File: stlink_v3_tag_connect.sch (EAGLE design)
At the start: 10 parts, among them CON1 STLINK_V3_HAT_SWD/JTAG_MINIMAL, J1 RJ12, U1 SN74LVC2T45DCU

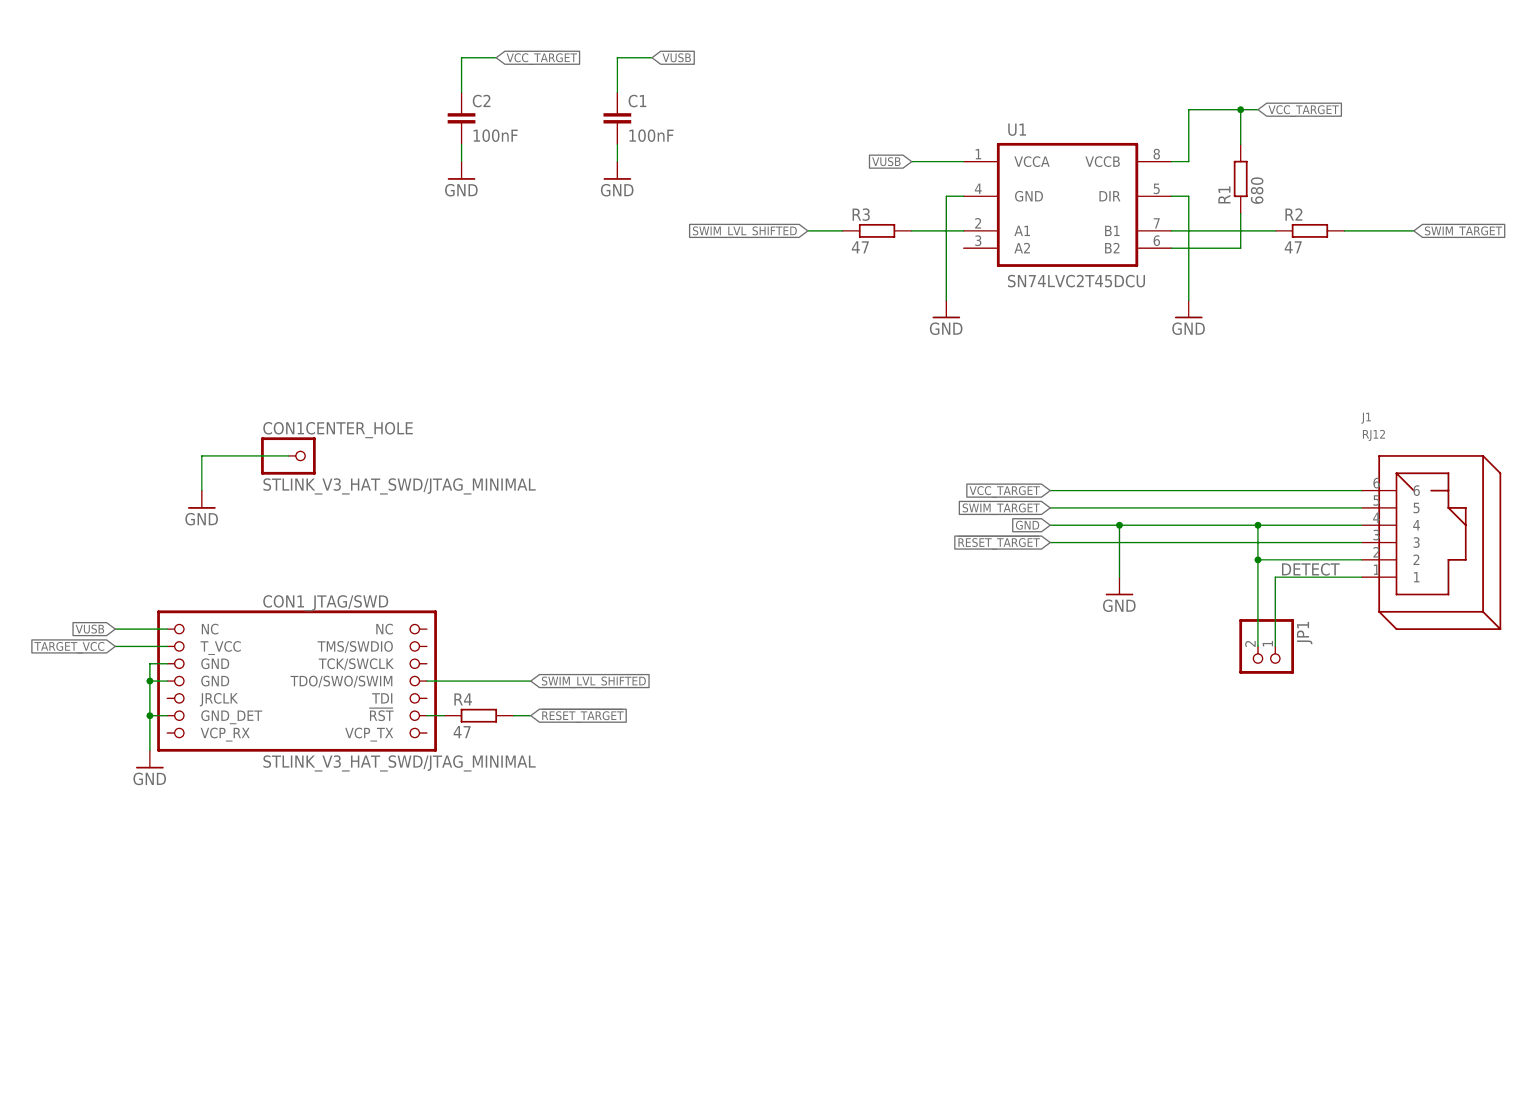
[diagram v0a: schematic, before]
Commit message: Fix missing SWIM data line back to the StLink
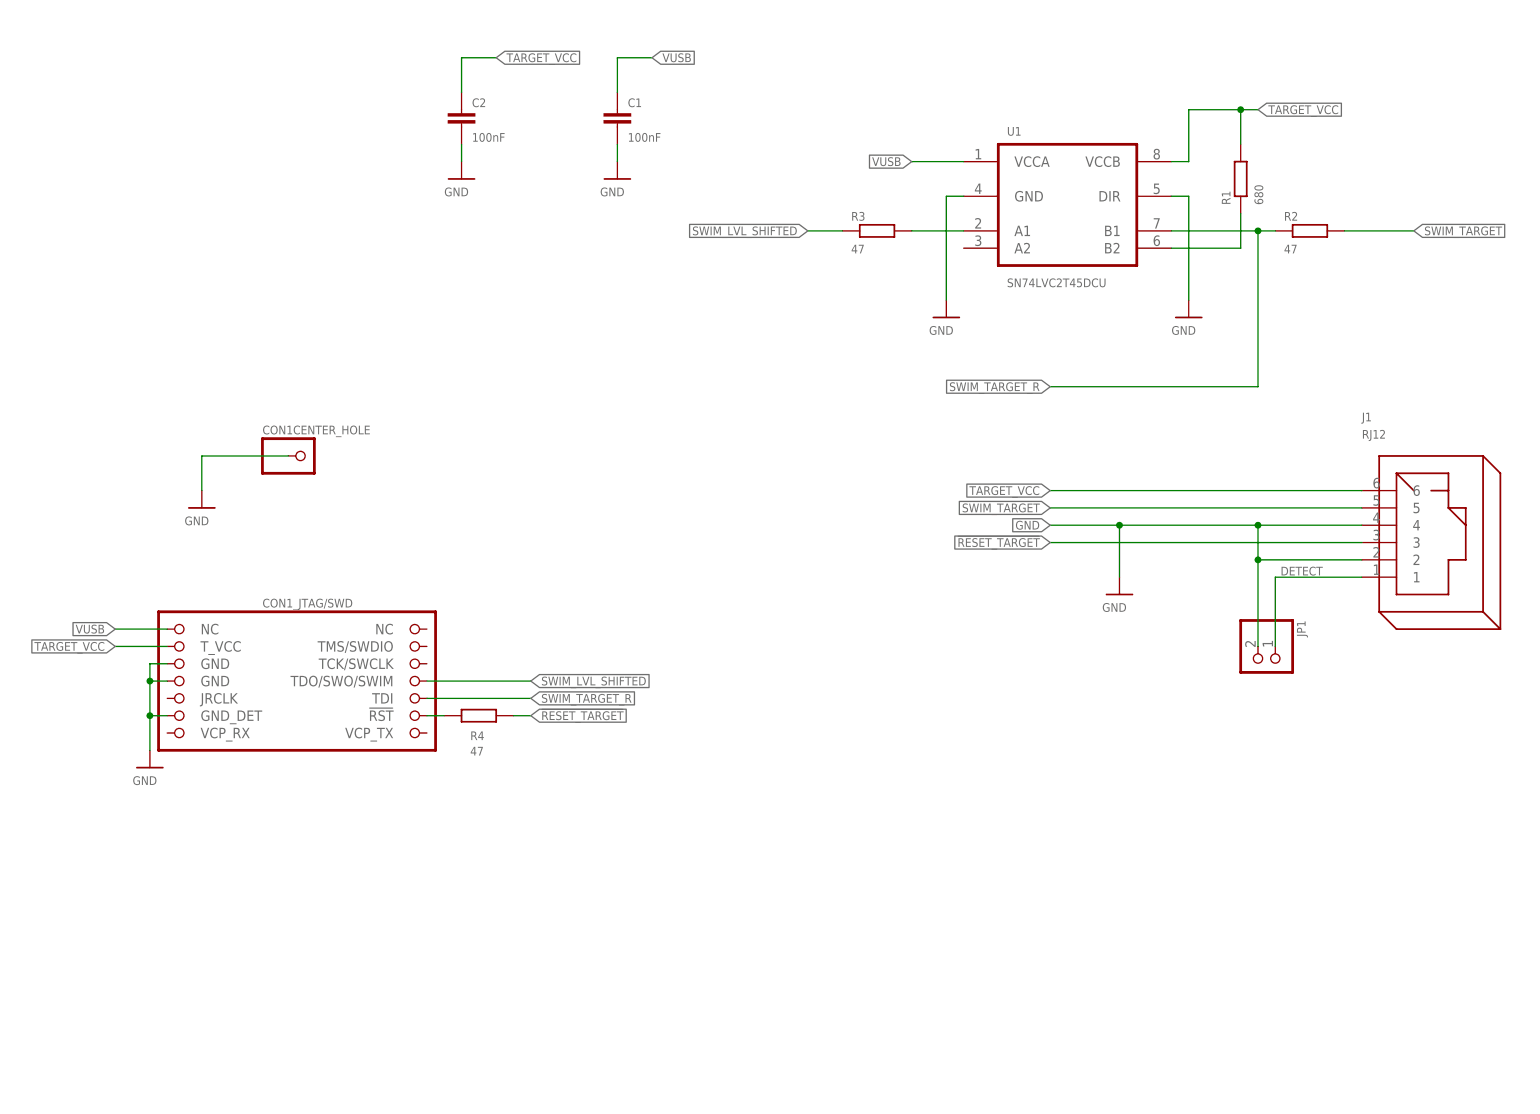
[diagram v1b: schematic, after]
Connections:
- removed net VCC_TARGET: C2.1, J1.6, R1.2, U1.VCCB
- net SWIM_TARGET_R: now also CON1_JTAG/SWD.TDI
- net TARGET_VCC: now also C2.1, J1.6, R1.2, U1.VCCB

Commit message: Added SCH in PNG
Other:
- note added: "STLinkV3 SWIM to Tag connect hat (based on reverse engineering MB1440)"
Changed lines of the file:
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@@
 <?xml version="1.0" encoding="utf-8"?>
 <!DOCTYPE eagle SYSTEM "eagle.dtd">
-<eagle version="9.2.2">
+<eagle version="9.3.2">
 <drawing>
 <settings>
@@
 <layer number="101" name="Patch_Top" color="12" fill="4" visible="yes" active="yes"/>
 <layer number="102" name="Vscore" color="7" fill="1" visible="yes" active="yes"/>
+<layer number="103" name="ATT_MISO" color="7" fill="1" visible="yes" active="yes"/>
 <layer number="104" name="Name" color="7" fill="1" visible="yes" active="yes"/>
+<layer number="105" name="Beschreib" color="7" fill="1" visible="yes" active="yes"/>
+<layer number="106" name="BGA-Top" color="7" fill="1" visible="yes" active="yes"/>
+<layer number="107" name="BD-Top" color="7" fill="1" visible="yes" active="yes"/>
+<layer number="108" name="centerline" color="7" fill="1" visible="yes" active="yes"/>
 <layer number="116" name="Patch_BOT" color="9" fill="4" visible="yes" active="yes"/>
 <layer number="121" name="_tsilk" color="7" fill="1" visible="yes" active="yes"/>
 <layer number="122" name="_bsilk" color="7" fill="1" visible="yes" active="yes"/>
 <layer number="126" name="_bNames" color="5" fill="1" visible="yes" active="yes"/>
+<layer number="131" name="prix" color="7" fill="1" visible="yes" active="yes"/>
+<layer number="132" name="test" color="7" fill="1" visible="yes" active="yes"/>
 <layer number="151" name="HeatSink" color="7" fill="1" visible="yes" active="yes"/>
 <layer number="200" name="200bmp" color="1" fill="10" visible="no" active="no"/>
@@
 <sheet>
 <plain>
+<text x="162.56" y="22.86" size="1.778" layer="94" font="vector" align="top-left">STLinkV3 SWIM to
+Tag connect hat
+(based on reverse engineering MB1440)</text>
 </plain>
 <instances>
@@
 <segment>
 <pinref part="U1" gate="G$1" pin="VCCA"/>
-<wire x1="149.86" y1="152.4" x2="142.24" y2="152.4" width="0.1524" layer="91"/>
-<label x="142.24" y="152.4" size="1.27" layer="95" font="vector" ratio="10" rot="R180" xref="yes"/>
-</segment>
-<segment>
+<wire x1="149.86" y1="152.4" x2="127" y2="152.4" width="0.1524" layer="91"/>
+<label x="127" y="152.4" size="1.27" layer="95" font="vector" ratio="10" rot="R180" xref="yes"/>
+</segment>
+<segment>

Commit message: Sch prettify
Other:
- moved on the sheet: CON1CENTER_HOLE
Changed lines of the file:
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@@
 <part name="CON1" library="stlinkv3" deviceset="STLINK_V3_HAT_SWD/JTAG_MINIMAL" device=""/>
 <part name="GND1" library="supply1" deviceset="GND" device=""/>
+<part name="P+1" library="supply1" deviceset="VUSB" device=""/>
+<part name="P+2" library="supply1" deviceset="VUSB" device=""/>
+<part name="U$1" library="supply1" deviceset="TARGET_VCC" device=""/>
+<part name="U$2" library="supply1" deviceset="TARGET_VCC" device=""/>
+<part name="U$3" library="supply1" deviceset="TARGET_VCC" device=""/>
 </parts>
 <sheets>
@@
 <attribute name="SHEET_HEADLINE" x="162.56" y="20.32" size="1.778" layer="94" font="vector"/>
 </instance>
-<instance part="GND2" gate="1" x="30.48" y="63.5" smashed="yes">
-<attribute name="VALUE" x="27.94" y="60.96" size="1.27" layer="96" font="vector"/>
+<instance part="GND2" gate="1" x="27.94" y="63.5" smashed="yes">
+<attribute name="VALUE" x="25.4" y="60.96" size="1.27" layer="96" font="vector"/>
 </instance>
 <instance part="J1" gate="G$1" x="218.44" y="99.06" smashed="yes">
@@
 <attribute name="NAME" x="46.99" y="86.995" size="1.27" layer="95" font="vector"/>
 </instance>
-<instance part="CON1" gate="CENTER_HOLE" x="53.34" y="109.22" smashed="yes">
-<attribute name="NAME" x="46.99" y="112.395" size="1.27" layer="95" font="vector"/>
+<instance part="CON1" gate="CENTER_HOLE" x="38.1" y="116.84" smashed="yes" rot="R90">
+<attribute name="NAME" x="31.75" y="120.015" size="1.27" layer="95" font="vector"/>
 </instance>
 <instance part="GND1" gate="1" x="38.1" y="101.6" smashed="yes">
 <attribute name="VALUE" x="35.56" y="99.06" size="1.27" layer="96" font="vector"/>
+</instance>
+<instance part="P+1" gate="G$1" x="99.06" y="170.18" smashed="yes">
+<attribute name="VALUE" x="99.06" y="171.45" size="1.778" layer="96" align="bottom-center"/>
+</instance>
+<instance part="P+2" gate="G$1" x="147.32" y="165.1" smashed="yes">
+<attribute name="VALUE" x="147.32" y="166.37" size="1.778" layer="96" align="bottom-center"/>
+</instance>
+<instance part="U$1" gate="G$1" x="76.2" y="167.64" smashed="yes">
+<attribute name="VALUE" x="76.2" y="171.45" size="1.778" layer="96" align="bottom-center"/>
+</instance>
+<instance part="U$2" gate="G$1" x="190.5" y="162.56" smashed="yes">
+<attribute name="VALUE" x="190.5" y="166.37" size="1.778" layer="96" align="bottom-center"/>
+</instance>
+<instance part="U$3" gate="G$1" x="193.04" y="106.68" smashed="yes">
+<attribute name="VALUE" x="193.04" y="110.49" size="1.778" layer="96" align="bottom-center"/>
 </instance>
 </instances>
@@
 <net name="GND" class="0">
 <segment>
-<wire x1="33.02" y1="76.2" x2="30.48" y2="76.2" width="0.1524" layer="91"/>
+<wire x1="33.02" y1="76.2" x2="27.94" y2="76.2" width="0.1524" layer="91"/>
 <pinref part="GND2" gate="1" pin="GND"/>
-<wire x1="30.48" y1="76.2" x2="30.48" y2="71.12" width="0.1524" layer="91"/>
-<wire x1="30.48" y1="71.12" x2="30.48" y2="66.04" width="0.1524" layer="91"/>
-<wire x1="33.02" y1="78.74" x2="30.48" y2="78.74" width="0.1524" layer="91"/>
-<wire x1="30.48" y1="78.74" x2="30.48" y2="76.2" width="0.1524" layer="91"/>
-<junction x="30.48" y="76.2"/>
+<wire x1="27.94" y1="76.2" x2="27.94" y2="71.12" width="0.1524" layer="91"/>
+<wire x1="27.94" y1="71.12" x2="27.94" y2="66.04" width="0.1524" layer="91"/>
+<wire x1="33.02" y1="78.74" x2="27.94" y2="78.74" width="0.1524" layer="91"/>
+<wire x1="27.94" y1="78.74" x2="27.94" y2="76.2" width="0.1524" layer="91"/>
+<junction x="27.94" y="76.2"/>
 <pinref part="CON1" gate="_JTAG/SWD" pin="GND@1"/>
 <pinref part="CON1" gate="_JTAG/SWD" pin="GND@2"/>
 <pinref part="CON1" gate="_JTAG/SWD" pin="GND_DET"/>
-<wire x1="33.02" y1="71.12" x2="30.48" y2="71.12" width="0.1524" layer="91"/>
-<junction x="30.48" y="71.12"/>
+<wire x1="33.02" y1="71.12" x2="27.94" y2="71.12" width="0.1524" layer="91"/>
+<junction x="27.94" y="71.12"/>
 </segment>
 <segment>
@@
 <segment>
 <pinref part="CON1" gate="CENTER_HOLE" pin="1"/>
-<wire x1="50.8" y1="109.22" x2="38.1" y2="109.22" width="0.1524" layer="91"/>
+<wire x1="38.1" y1="114.3" x2="38.1" y2="109.22" width="0.1524" layer="91"/>
 <pinref part="GND1" gate="1" pin="GND"/>
 <wire x1="38.1" y1="109.22" x2="38.1" y2="104.14" width="0.1524" layer="91"/>
@@
 <segment>
 <pinref part="U1" gate="G$1" pin="VCCA"/>
-<wire x1="149.86" y1="152.4" x2="127" y2="152.4" width="0.1524" layer="91"/>
-<label x="127" y="152.4" size="1.27" layer="95" font="vector" ratio="10" rot="R180" xref="yes"/>
+<wire x1="149.86" y1="152.4" x2="147.32" y2="152.4" width="0.1524" layer="91"/>
+<pinref part="P+2" gate="G$1" pin="VUSB"/>
+<wire x1="147.32" y1="162.56" x2="147.32" y2="152.4" width="0.1524" layer="91"/>
 </segment>
 <segment>
 <pinref part="C1" gate="G$1" pin="1"/>
 <wire x1="99.06" y1="162.56" x2="99.06" y2="167.64" width="0.1524" layer="91"/>
-<wire x1="99.06" y1="167.64" x2="104.14" y2="167.64" width="0.1524" layer="91"/>
-<label x="104.14" y="167.64" size="1.27" layer="95" font="vector" ratio="10" xref="yes"/>
+<pinref part="P+1" gate="G$1" pin="VUSB"/>
 </segment>
 </net>
@@
 <pinref part="R1" gate="G$1" pin="2"/>
 <wire x1="190.5" y1="160.02" x2="190.5" y2="154.94" width="0.1524" layer="91"/>
-<label x="193.04" y="160.02" size="1.27" layer="95" font="vector" ratio="10" xref="yes"/>
-<wire x1="190.5" y1="160.02" x2="193.04" y2="160.02" width="0.1524" layer="91"/>
 <junction x="190.5" y="160.02"/>
+<pinref part="U$2" gate="G$1" pin="TARGET_VCC"/>
+<wire x1="190.5" y1="162.56" x2="190.5" y2="160.02" width="0.1524" layer="91"/>
 </segment>
 <segment>
 <pinref part="J1" gate="G$1" pin="6"/>
-<wire x1="208.28" y1="104.14" x2="162.56" y2="104.14" width="0.1524" layer="91"/>
-<label x="162.56" y="104.14" size="1.27" layer="95" font="vector" ratio="10" rot="R180" xref="yes"/>
+<wire x1="208.28" y1="104.14" x2="193.04" y2="104.14" width="0.1524" layer="91"/>
+<pinref part="U$3" gate="G$1" pin="TARGET_VCC"/>
+<wire x1="193.04" y1="106.68" x2="193.04" y2="104.14" width="0.1524" layer="91"/>
 </segment>
 <segment>
 <pinref part="C2" gate="G$1" pin="1"/>
 <wire x1="76.2" y1="162.56" x2="76.2" y2="167.64" width="0.1524" layer="91"/>
-<wire x1="76.2" y1="167.64" x2="81.28" y2="167.64" width="0.1524" layer="91"/>
-<label x="81.28" y="167.64" size="1.27" layer="95" font="vector" ratio="10" xref="yes"/>
-</segment>
-</net>
+<pinref part="U$1" gate="G$1" pin="TARGET_VCC"/>
+</segment>
+</net>
